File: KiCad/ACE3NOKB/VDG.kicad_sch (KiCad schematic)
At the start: 40 parts, among them Q101 2N3904

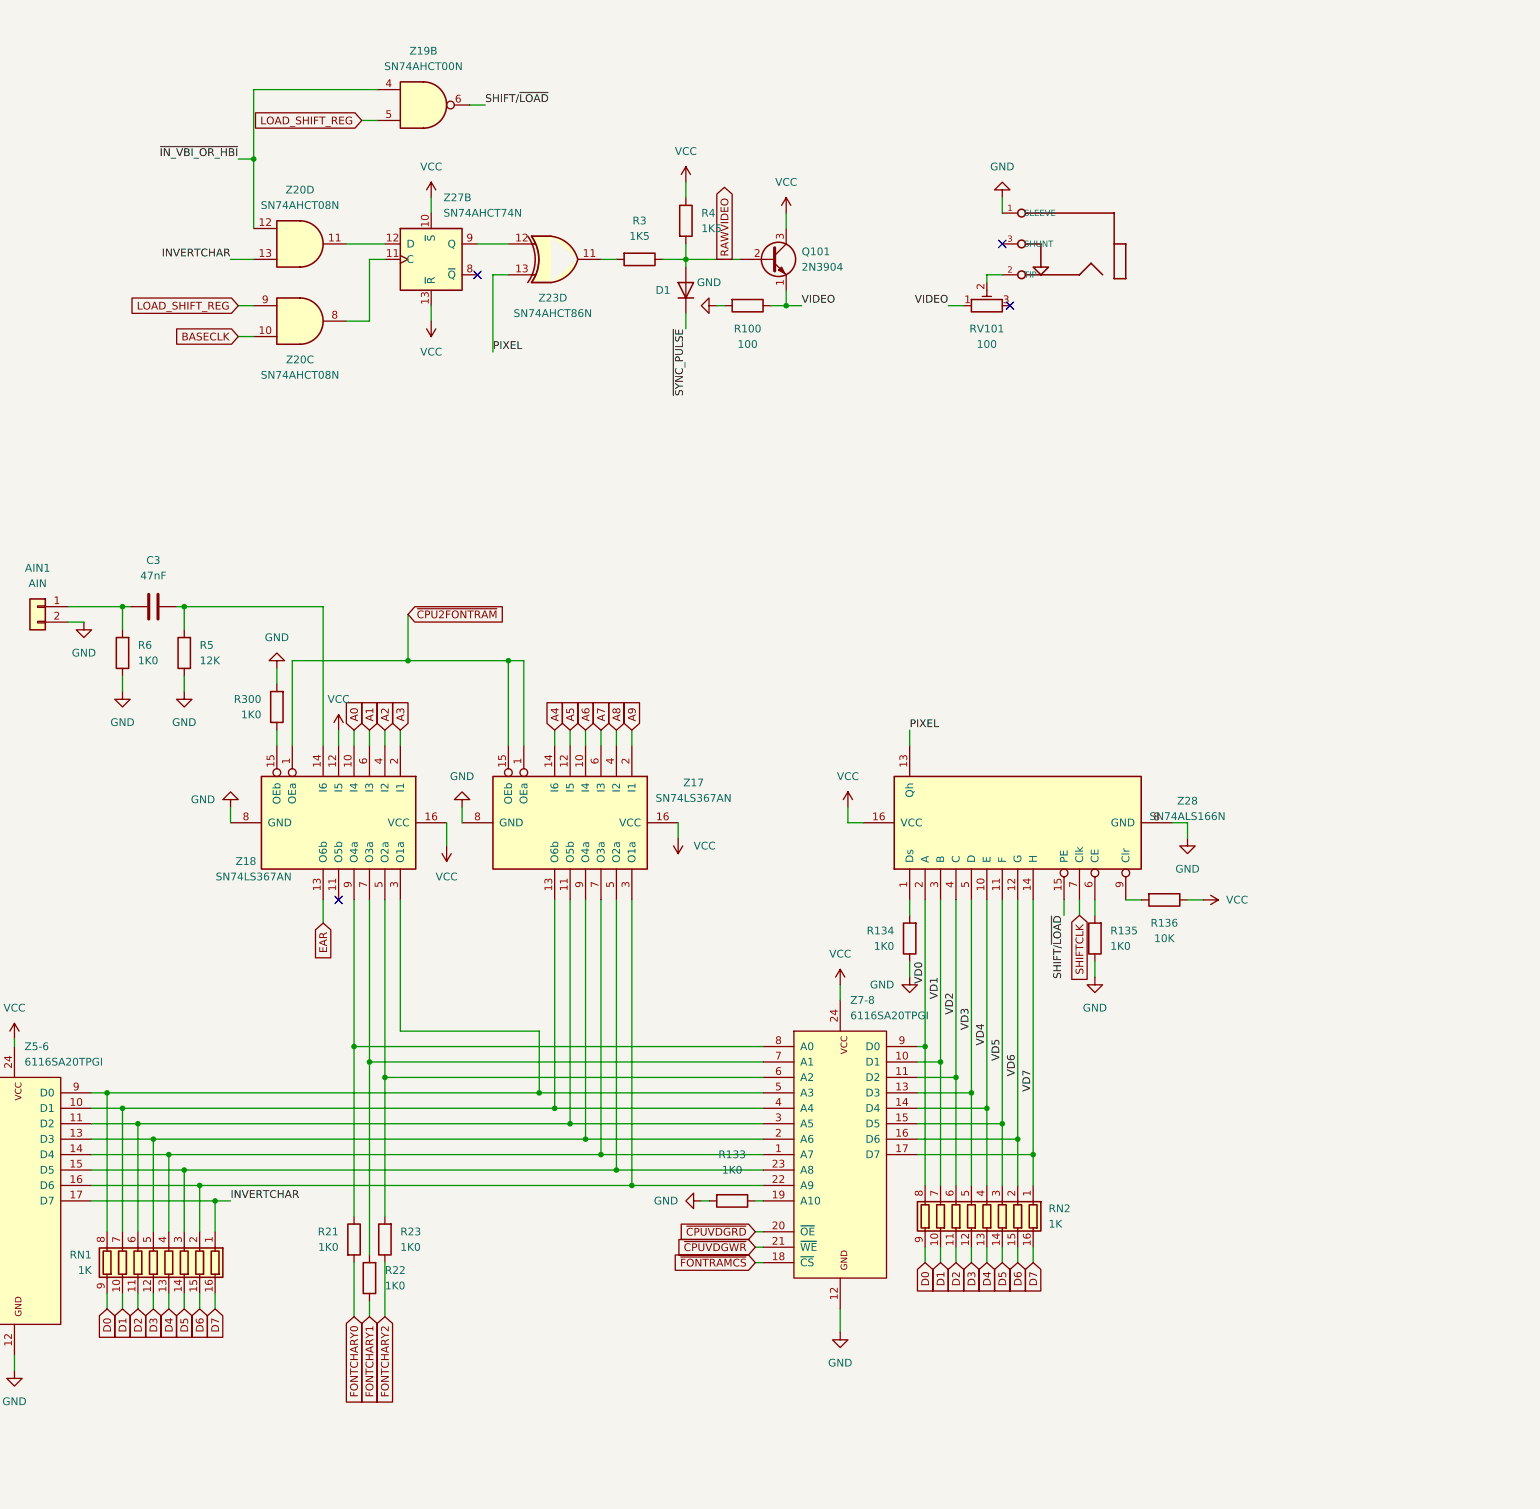
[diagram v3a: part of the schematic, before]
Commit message: Fix mistake with ROM Select.
Signed-off-by: John Bradley <flypie@rocketmail.com>
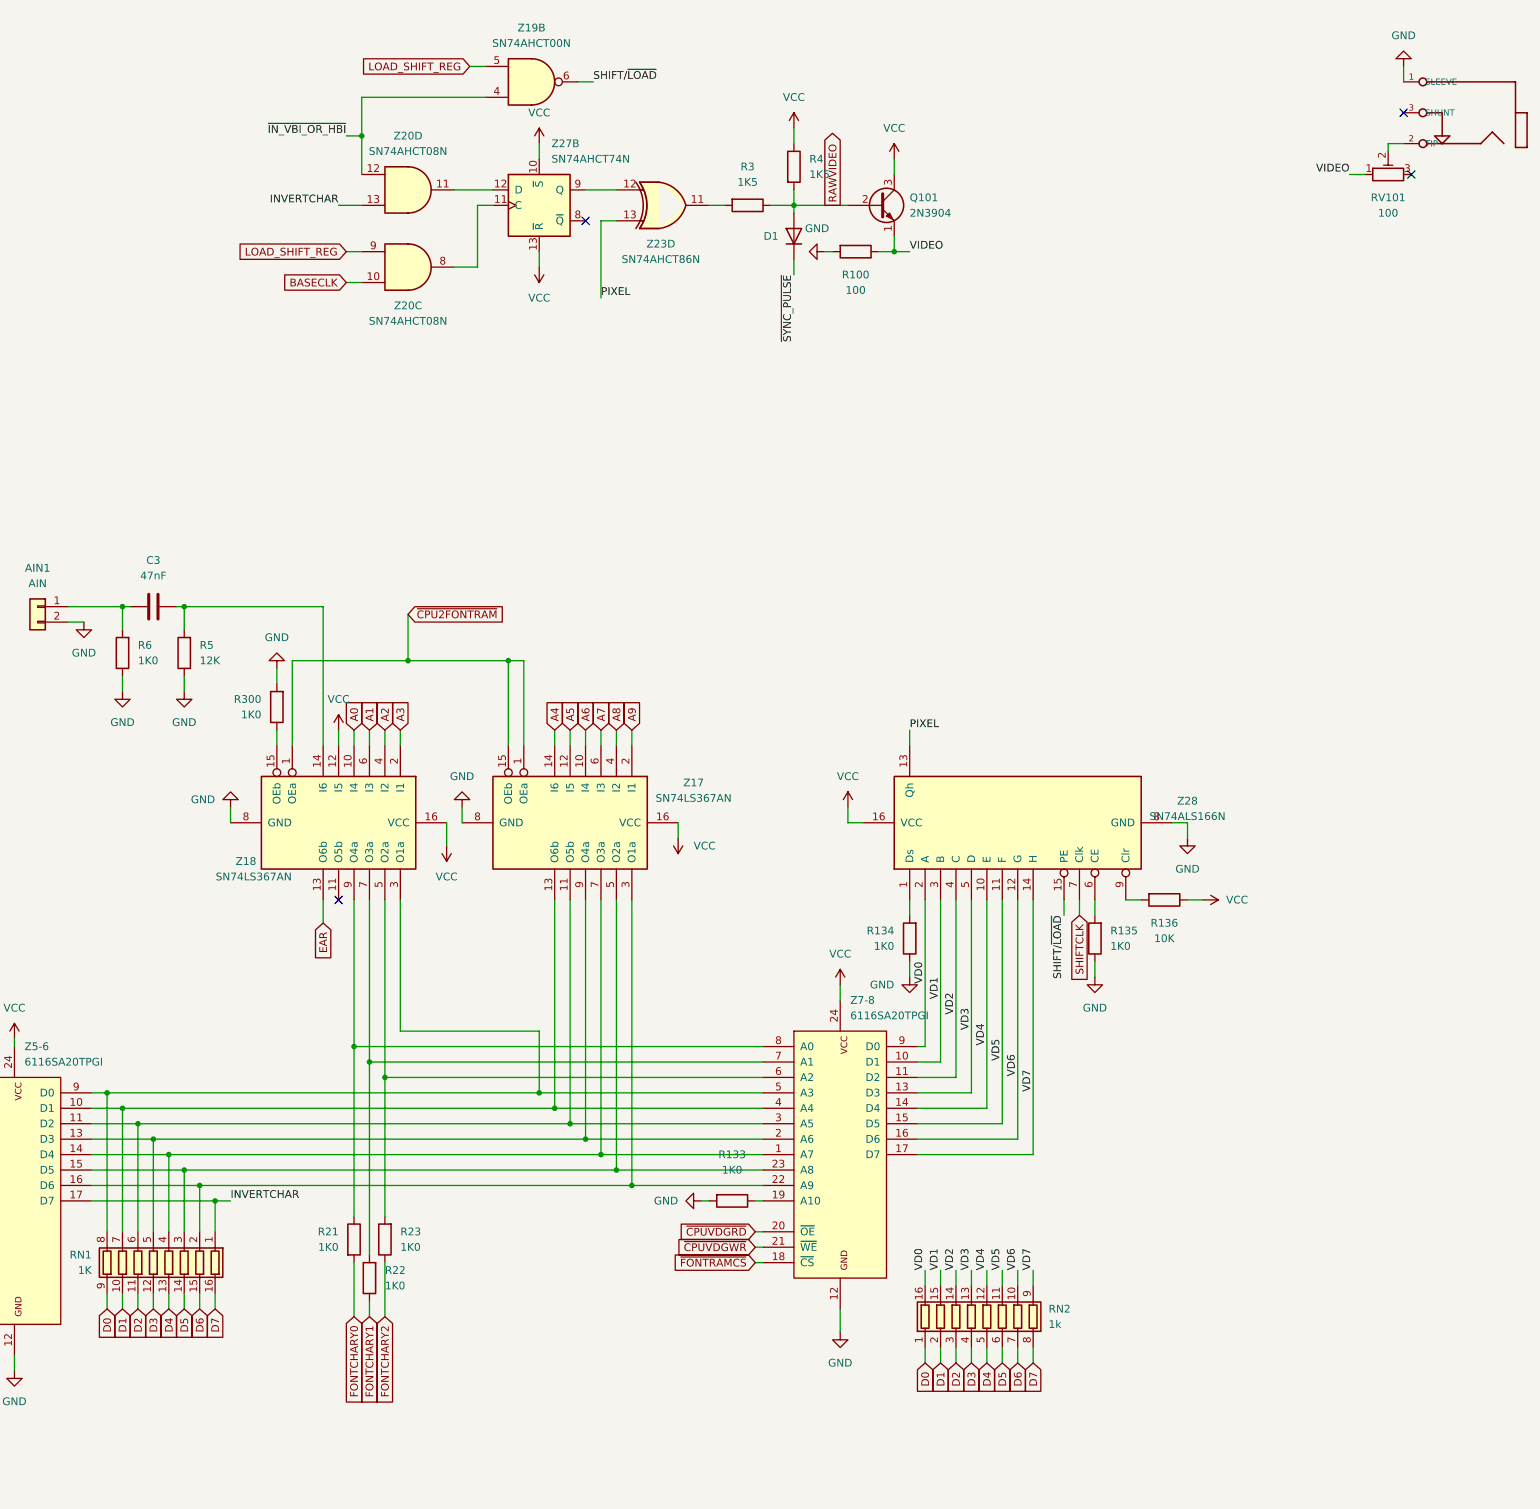
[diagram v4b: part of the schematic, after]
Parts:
- RN2: value 1K -> 1k
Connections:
- net D0: now also RN2.1 (R1.1); no longer RN2.9 (R8.2)
- net D1: now also RN2.2 (R2.1); no longer RN2.10 (R7.2)
- net D2: now also RN2.3 (R3.1); no longer RN2.11 (R6.2)
- net D3: now also RN2.4 (R4.1); no longer RN2.12 (R5.2)
- net D4: now also RN2.5 (R5.1); no longer RN2.13 (R4.2)
- net D5: now also RN2.6 (R6.1); no longer RN2.14 (R3.2)
- net D6: now also RN2.7 (R7.1); no longer RN2.15 (R2.2)
- net D7: now also RN2.8 (R8.1); no longer RN2.16 (R1.2)
- net VD0: now also RN2.16 (R1.2); no longer RN2.8 (R8.1)
- net VD1: now also RN2.15 (R2.2); no longer RN2.7 (R7.1)
- net VD2: now also RN2.14 (R3.2); no longer RN2.6 (R6.1)
- net VD3: now also RN2.13 (R4.2); no longer RN2.5 (R5.1)
- net VD4: now also RN2.12 (R5.2); no longer RN2.4 (R4.1)
- net VD5: now also RN2.11 (R6.2); no longer RN2.3 (R3.1)
- net VD6: now also RN2.10 (R7.2); no longer RN2.2 (R2.1)
- net VD7: now also RN2.9 (R8.2); no longer RN2.1 (R1.1)
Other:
- moved on the sheet: D1, Q101, R100, R3, R4, RV101, Z19B, Z20C, Z20D, Z23D, Z27B

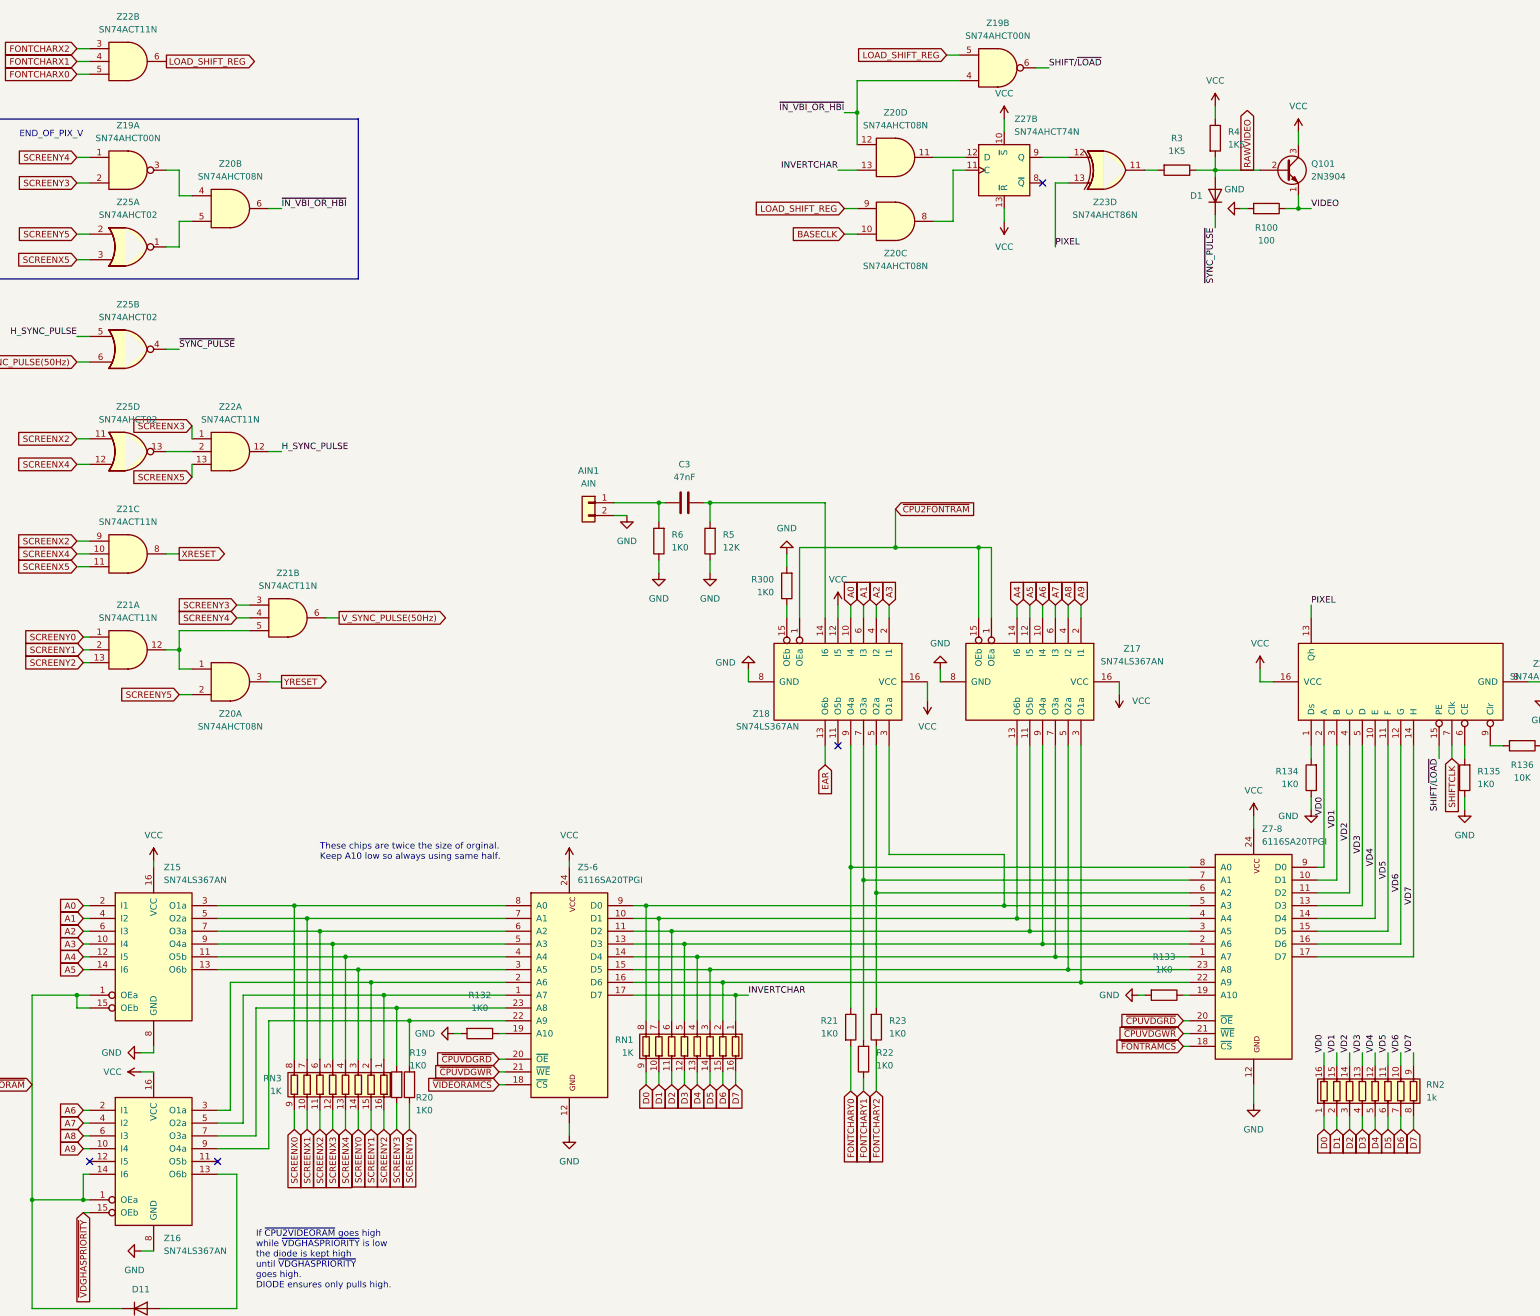
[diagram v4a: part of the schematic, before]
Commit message: Update to last expermintal version. Uses clock sythsiser and can be switched between full ACE compatible and inhanced IO. Should be able to switch between multiple ROM images tosred on the same chip.
Signed-off-by: John Bradley <flypie@rocketmail.com>
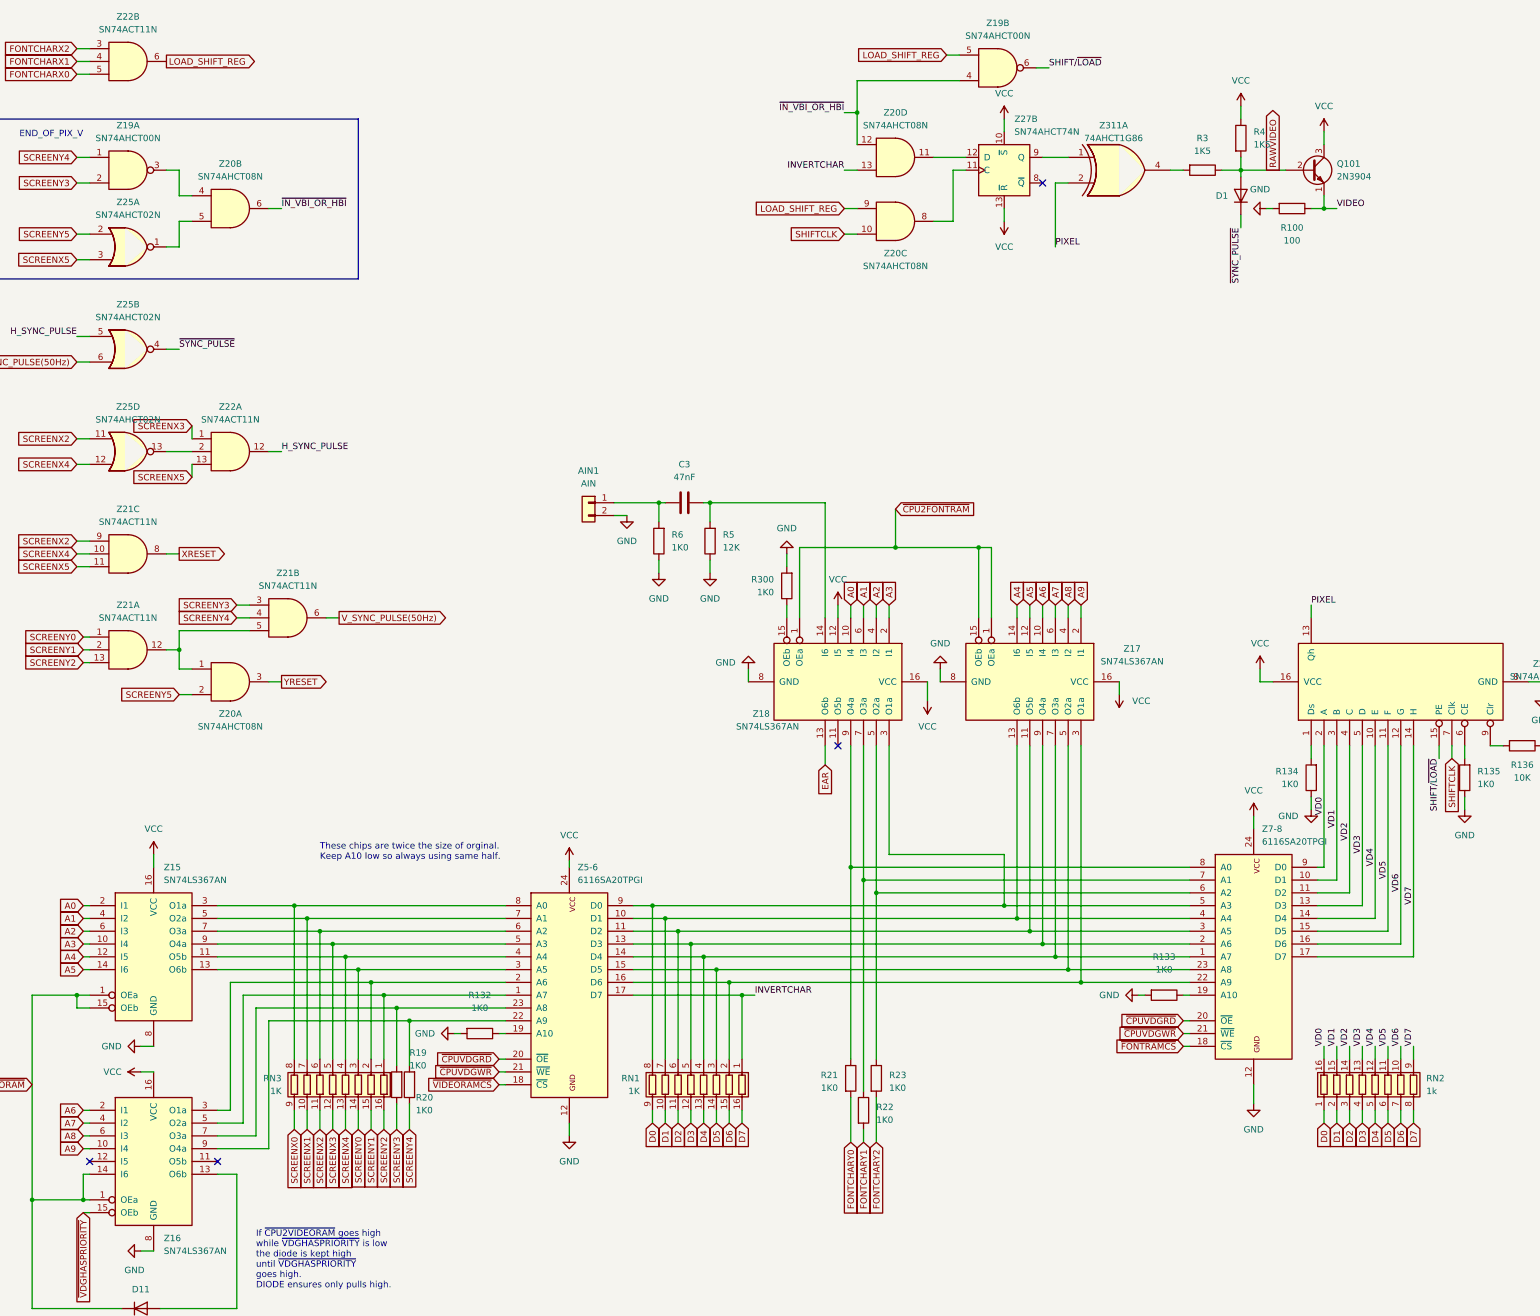
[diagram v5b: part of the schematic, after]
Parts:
- removed Z23: SN74AHCT86N, Package_DIP:DIP-14_W7.62mm, symbol 74xx:74LS86
- added Z311: 74AHCT1G86, Package_TO_SOT_SMD:SOT-23-5, symbol 74xGxx:74AHCT1G86
- COMP1: Field4 (none) -> Conn Rca Jack Mono 3.2mm r/a; Field5 (none) -> None; Field6 (none) -> PJRAN1X1U03AUX; Field7 (none) -> Unavailable; Field8 (none) -> Switchcraft Inc.
- Q101: footprint Package_TO_SOT_THT:TO-92_Inline -> Package_TO_SOT_THT:TO-92_Wide
- Z25: value SN74AHCT02 -> SN74AHCT02N
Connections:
- net BASECLK is gone; now on net SHIFTCLK: Z20.10
- net FONTCHARY1: now also R22.2; no longer R22.1
- net FONTCHARY2: now also R23.2; no longer R23.1
- net PIXEL: now also Z311.2
- net at Z18.7 (O3a), Z7-8.7 (A1): now also R22.1; no longer R22.2
- net at Z18.5 (O2a), Z7-8.6 (A2): now also R23.1; no longer R23.2
- net at Z27.9 (Q): now also Z311.1
- net at R3.2: now also Z311.4
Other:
- moved on the sheet: D1, Q101, R100, R21, R22, R23, R3, R4, RN1, RN2
